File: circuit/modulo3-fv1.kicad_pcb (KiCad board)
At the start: 2 copper layers, 90 x 80 mm, 55 parts, among them J1 CONN_01X04, J2 CONN_01X10, J3 CONN_01X03, J4 HOLE, J5 HOLE, U1 OPA1642, U10 TLE2426, U2 PWR_CONN, U3 FV-1, U5 LM1117 3V3, U7 AD5142A, Y1 32768Hz

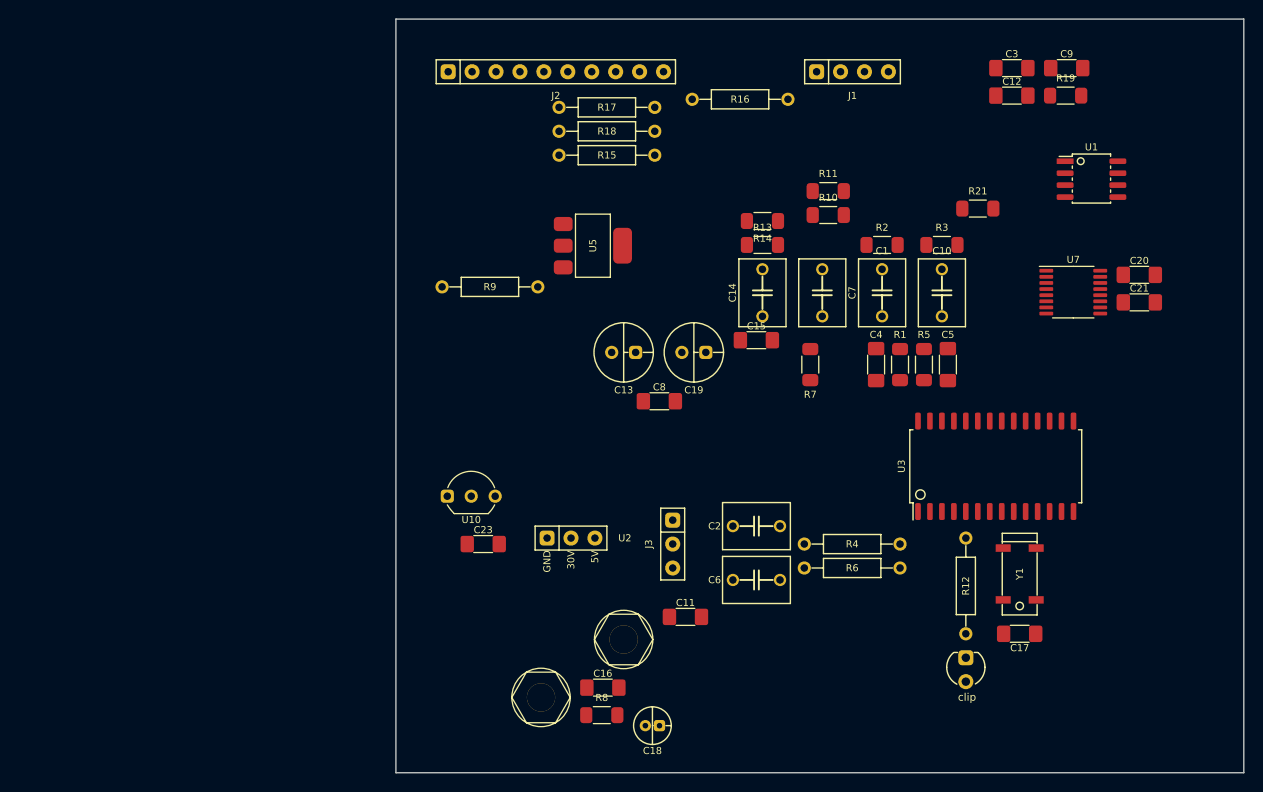
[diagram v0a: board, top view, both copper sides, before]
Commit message: mcu board; fv1 board tracing
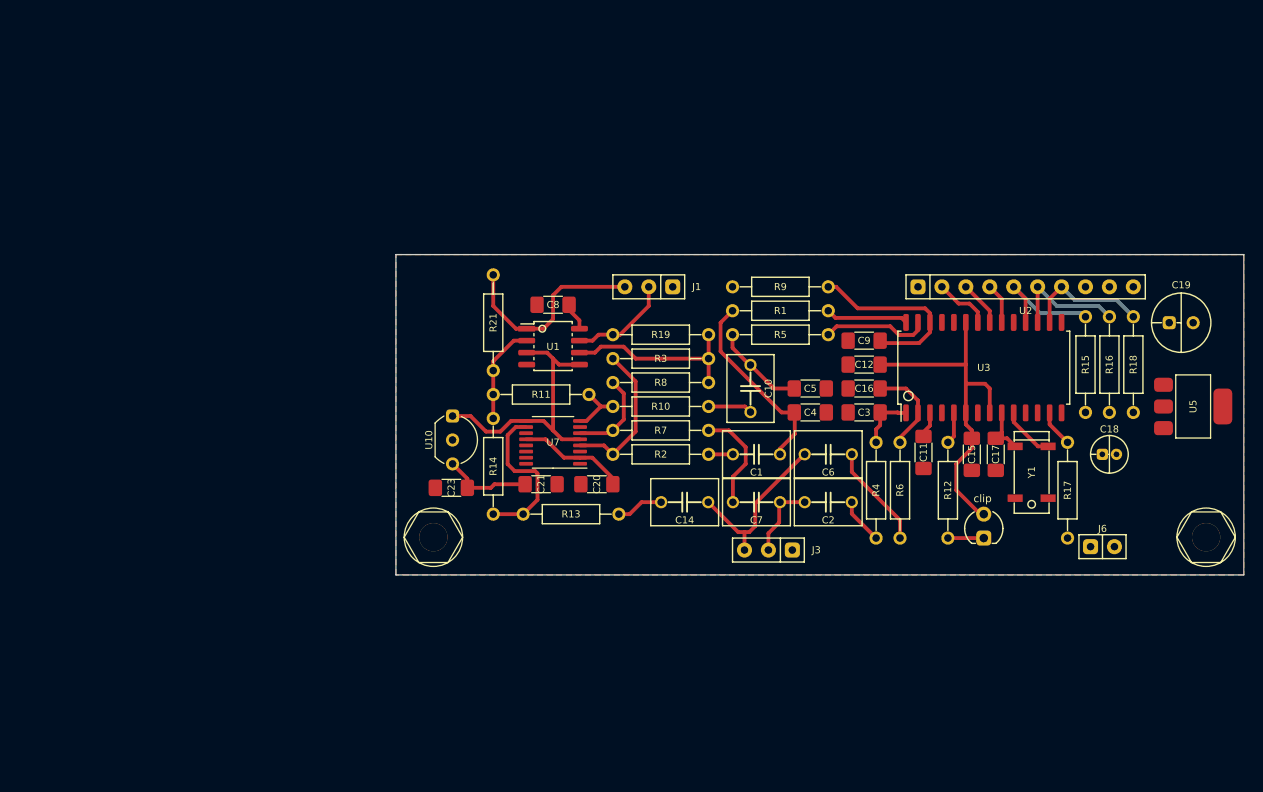
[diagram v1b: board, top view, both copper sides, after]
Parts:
- removed C13: 10µF, myAmp:CPOL_D6.3_P2.5
- removed J2: CONN_01X10, myAmp:PIN_1x10
- added J6: CONN_01X02, myAmp:PIN_1x02, F.Cu at (165.0, 86.0)
- J1: value CONN_01X04 -> CONN_01X03; footprint myAmp:PIN_1x04 -> myAmp:PIN_1x03
- R1, R10, R11, R13, R14, R19, R2, R21, R3, R5, R7, R8: footprint myAmp:R_1206 -> myAmp:R_10MM
- U2: value PWR_CONN -> FV1_CONN; footprint myAmp:PWR_CONN -> myAmp:PIN_1x10
- moved C21 66.4 mm to (105.4, 79.4), turned to 180 degrees
- moved U5 66.0 mm to (174.6, 71.1)
- moved R17 63.6 mm to (161.3, 80.0), turned to -90 degrees
- moved J4 62.8 mm to (176.0, 85.0)
- moved C20 61.7 mm to (111.3, 79.4)
- moved R18 61.1 mm to (168.3, 66.7), turned to -90 degrees
- moved U1 59.9 mm to (106.7, 64.8)
- moved U7 57.5 mm to (106.7, 74.9), turned to 180 degrees
- moved C18 56.4 mm to (165.7, 76.2), turned to 180 degrees
- moved R15 55.4 mm to (163.2, 66.7), turned to -90 degrees
- moved U2 55.1 mm to (156.8, 58.4)
- moved R21 52.8 mm to (100.3, 62.2), turned to 90 degrees
- moved C19 51.8 mm to (173.4, 62.2), turned to 180 degrees
- moved R19 49.9 mm to (118.1, 63.5), turned to 180 degrees
- moved R16 48.3 mm to (165.7, 66.7), turned to 90 degrees
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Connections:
- J1 pad 3: GND -> /OUTR
- U2 pad 2: +24V -> /POT2
- U2 pad 3: +5V -> /POT1
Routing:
- net +3V3: track 0.00 -> 48.7 mm
- net VGND: track 0.00 -> 29.2 mm
- net /OUTR: track 0.00 -> 21.6 mm
- net /FVL: track 0.00 -> 20.5 mm
- net /REFP: track 0.00 -> 19.8 mm
- net Net-(R19-Pad1): track 0.00 -> 19.6 mm
- net INR: track 0.00 -> 18.3 mm
- net /B2: track 0.00 -> 17.1 mm
- net /A1: track 0.00 -> 16.0 mm
- net /S2: track 0.00 -> 13.2 mm
- net /S0: track 0.00 -> 13.2 mm
- net /S1: track 0.00 -> 12.7 mm
- net +5V: track 0.00 -> 12.5 mm
- net Net-(R5-Pad2): track 0.00 -> 11.3 mm
- net Net-(C7-Pad2): track 0.00 -> 11.1 mm
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- added copper zone on F.Cu, net GND
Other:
- board size 90 x 80 mm -> 90 x 34 mm

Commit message: general layout and board sizes
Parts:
- U2: footprint myAmp:PIN_1x10 -> myAmp:FV1_CONN
- moved J5 26.0 mm to (94.0, 59.0)
- moved J4 26.0 mm to (176.0, 59.0)
- moved C19 8.89 mm to (173.4, 71.1)
- moved U5 7.85 mm to (172.7, 78.7)
- moved U2 5.85 mm to (151.1, 57.1), turned to -90 degrees
- moved R13 2.36 mm to (108.6, 84.9)
- moved R21 1.91 mm to (100.3, 64.1)
- moved C1 1.91 mm to (128.3, 78.1)
- moved C10 1.91 mm to (127.6, 71.1)
- moved C11 1.91 mm to (146.0, 77.9)
- moved C12 1.91 mm to (139.7, 68.6)
- moved C14 1.91 mm to (120.7, 83.2)
- moved C15 1.91 mm to (151.1, 78.1)
- moved C16 1.91 mm to (139.7, 71.1)
- moved C17 1.91 mm to (153.7, 78.1)
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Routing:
- net /T0: track 3.92 -> 34.2 mm
- net /SCL: track 0.00 -> 17.3 mm
- net /S2: track 13.2 -> 27.7 mm
- net /S1: track 12.7 -> 26.0 mm
- net /S0: track 13.2 -> 25.5 mm
- net /SDA: track 0.00 -> 7.50 mm
- net /POT1: track 4.83 -> 12.0 mm
- net /POT2: track 6.03 -> 12.9 mm
- net /POT0: track 4.31 -> 11.1 mm
- net /B2: track 17.1 -> 17.7 mm
- net GND: vias 0 -> 3
- added copper zone on B.Cu, net GND

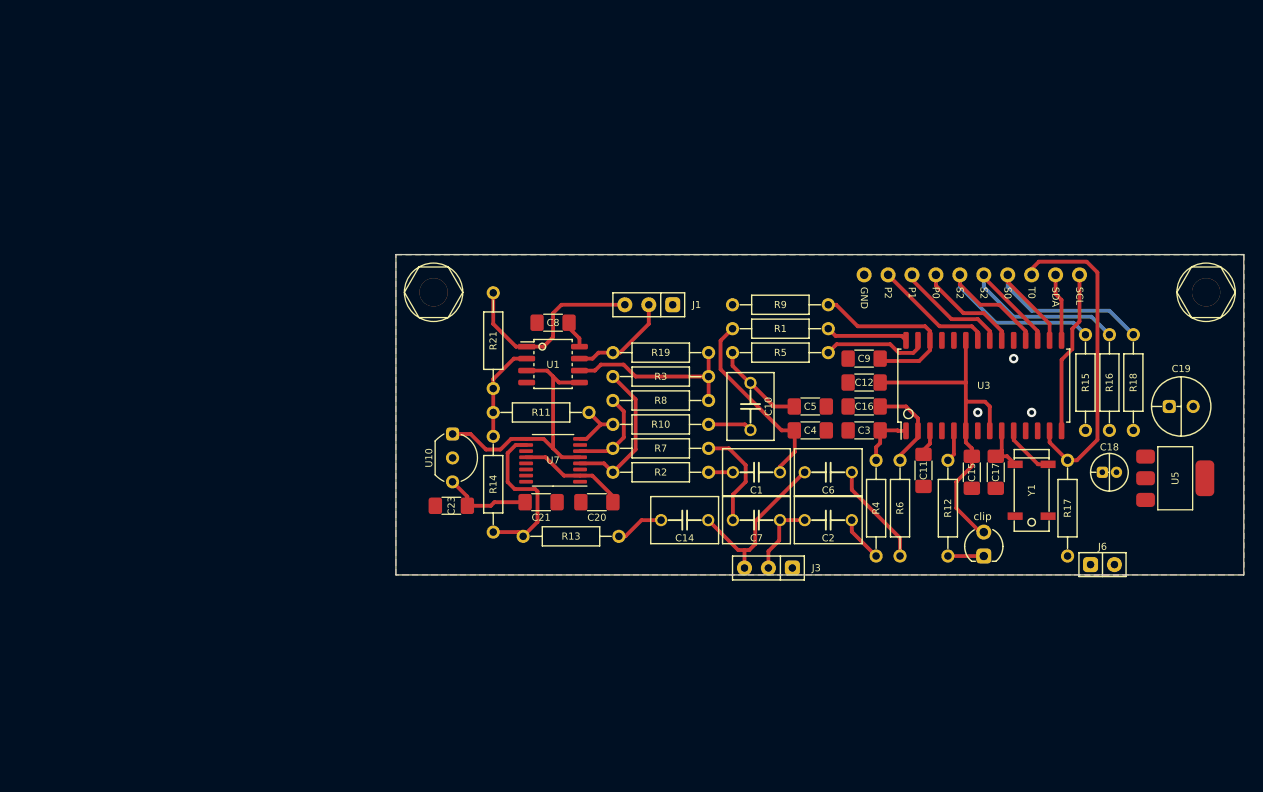
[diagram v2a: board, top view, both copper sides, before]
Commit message: got the pcs and holes sizes for mcu, poweamp and fv1
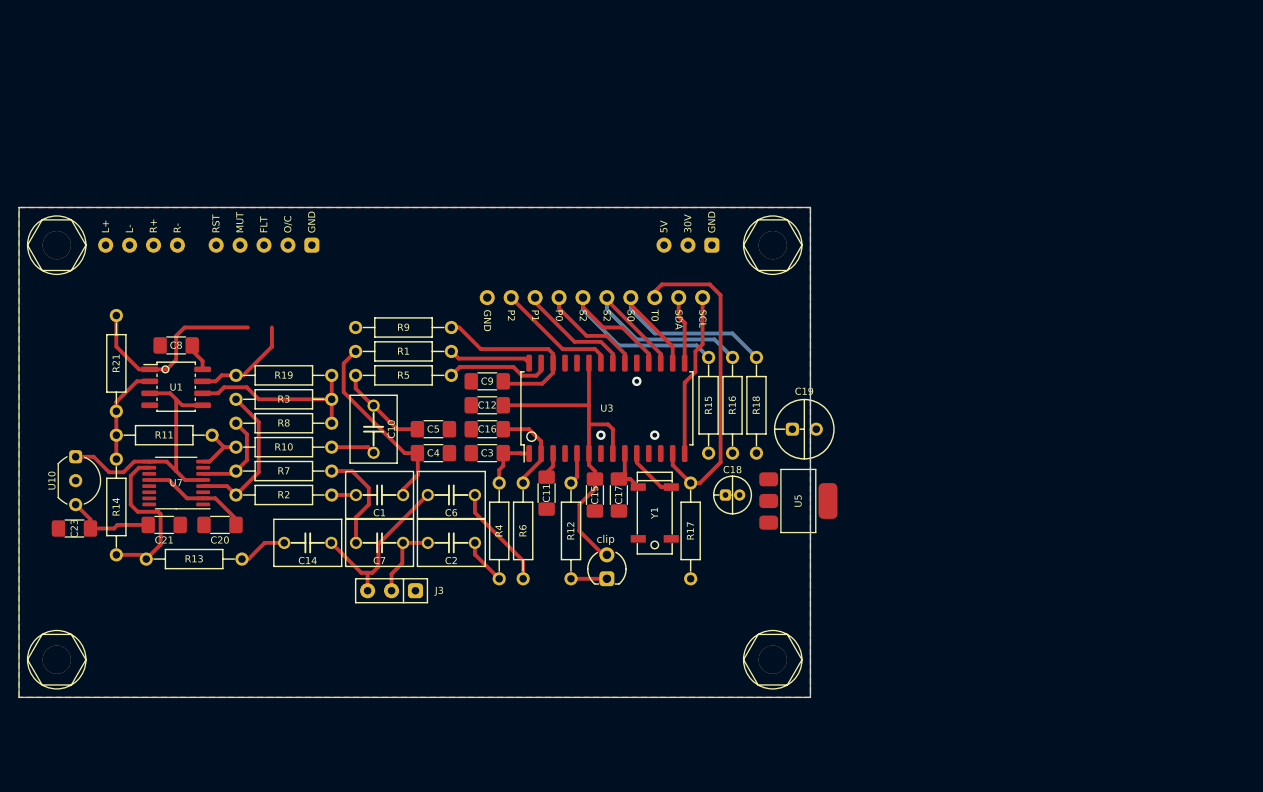
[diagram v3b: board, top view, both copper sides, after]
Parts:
- removed J1: CONN_01X03, myAmp:PIN_1x03
- removed J6: CONN_01X02, myAmp:PIN_1x02
- added J2: HOLE, myAmp:MountingHole, F.Cu at (54.0, 98.0)
- added J7: HOLE, myAmp:MountingHole, F.Cu at (130.0, 98.0)
- added U4: PWR_CONN, myAmp:PWR_CONN, F.Cu at (121.0, 54.0)
- added U6: DIFFAUDIO, myAmp:DIFFAUDIO, F.Cu at (63.0, 54.0)
- added U8: AMPCTRL, myAmp:AMPCTRL, F.Cu at (76.0, 54.0)
- moved J4 46.3 mm to (130.0, 54.0)
- moved J5 40.3 mm to (54.0, 54.0)
- moved C1 40.1 mm to (88.3, 80.5)
- moved C10 40.1 mm to (87.6, 73.5)
- moved C14 40.1 mm to (80.6, 85.6)
- moved C18 40.1 mm to (125.7, 80.5)
- moved C4 40.1 mm to (94.0, 76.1)
- moved C5 40.1 mm to (94.0, 73.5)
- moved C7 40.1 mm to (88.3, 85.6)
- moved C8 40.1 mm to (66.7, 64.6)
- moved D1 40.1 mm to (112.4, 88.1)
- moved R12 40.1 mm to (108.6, 84.3)
- moved R16 40.1 mm to (125.7, 71.0)
- moved U1 40.1 mm to (66.7, 69.1)
- moved U3 40.1 mm to (112.4, 71.3)
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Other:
- board size 90 x 34 mm -> 84 x 52 mm

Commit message: fv-1 mostly done; power progressed
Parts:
- removed J3: CONN_01X03, myAmp:PIN_1x03
- added U9: PREAMP, myAmp:PREAMP_CONN, F.Cu at (80.0, 98.0)
- moved R16 36.4 mm to (92.1, 57.1), turned to 0 degrees
- moved R15 33.1 mm to (92.1, 59.7), turned to 180 degrees
- moved R18 25.1 mm to (107.3, 57.1), turned to 0 degrees
- moved C18 22.2 mm to (120.2, 59.0), turned to 0 degrees
- moved U5 16.1 mm to (125.0, 67.0), turned to -90 degrees
- moved C14 15.7 mm to (66.6, 92.7)
- moved R13 13.3 mm to (55.2, 87.0), turned to 90 degrees
- moved U2 11.6 mm to (101.0, 54.0), turned to 0 degrees
- moved R14 9.05 mm to (55.2, 74.3)
- moved C19 8.63 mm to (125.0, 75.7), turned to -90 degrees
- moved U10 8.27 mm to (64.1, 77.5), turned to 180 degrees
- moved C23 7.90 mm to (59.1, 76.8), turned to 90 degrees
- moved C21 7.12 mm to (58.4, 85.1), turned to 90 degrees
- moved U7 5.23 mm to (64.1, 83.8)
- moved C7 4.58 mm to (85.1, 88.9)
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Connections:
- R12 pad 2: Net-(R12-Pad2) -> /CLIP
- U2 pad 1: GND -> /POT2
- U2 pad 10: /SCL -> /CLIP
- U2 pad 2: /POT2 -> /POT1
- U2 pad 3: /POT1 -> /POT0
- U2 pad 4: /POT0 -> /S2
- U2 pad 5: /S2 -> /S1
- U2 pad 6: /S1 -> /S0
- U2 pad 7: /S0 -> /FV_SDA
- U2 pad 8: /T0 -> /FV_SCL
- U2 pad 9: /SDA -> /T0
- U3 pad 14: /SCL -> /FV_SCL
- U3 pad 15: /SDA -> /FV_SDA
- U3 pad 5: Net-(R12-Pad2) -> /CLIP
- U4 pad 2: unconnected-(U4-Pad2) -> /30V
- U7 pad 13: /SCL -> SCL
- U7 pad 14: /SDA -> SDA
- U8 pad 1: unconnected-(U8-Pad1) -> GND
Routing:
- net /30V: track 0.00 -> 86.9 mm
- net +5V: track 12.5 -> 95.3 mm
- net +3V3: track 48.7 -> 116.8 mm
- net /CLIP: track 0.00 -> 60.4 mm
- net /FV_SCL: track 0.00 -> 28.4 mm
- net INR: track 18.3 -> 45.7 mm
- net SCL: track 0.00 -> 22.8 mm
- net SDA: track 0.00 -> 20.0 mm
- net /FV_SDA: track 0.00 -> 19.5 mm
- net /SCL: track 17.3 -> 0.00 mm
- net /POT0: track 11.1 -> 27.6 mm
- net /POT1: track 12.0 -> 28.0 mm
- net /POT2: track 12.9 -> 28.4 mm
- net /B2: track 17.7 -> 8.68 mm
- net /OUTL: track 10.9 -> 19.0 mm
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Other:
- outline, holes or cut-outs redrawn

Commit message: lotsa things :)
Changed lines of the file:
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@@
         (effects (font (size 0.75 0.75) (thickness 0.15)))
     )
-    (fp_text user "CLP" (at 11.43 -1.27 90 unlocked) (layer "F.SilkS")
+    (fp_text user "T0" (at 8.89 -1.27 90 unlocked) (layer "F.SilkS")
+        (effects (font (size 0.75 0.75) (thickness 0.15)) (justify left))
+    )
+    (fp_text user "SDA" (at 3.81 -1.27 90 unlocked) (layer "F.SilkS")
+        (effects (font (size 0.75 0.75) (thickness 0.15)) (justify left))
+    )
+    (fp_text user "P1" (at -8.89 -1.27 90 unlocked) (layer "F.SilkS")
         (effects (font (size 0.75 0.75) (thickness 0.15)) (justify left))
     )
     (fp_text user "S0" (at 1.27 -1.27 90 unlocked) (layer "F.SilkS")
-        (effects (font (size 0.75 0.75) (thickness 0.15)) (justify left))
-    )
-    (fp_text user "P0" (at -6.35 -1.27 90 unlocked) (layer "F.SilkS")
         (effects (font (size 0.75 0.75) (thickness 0.15)) (justify left))
     )
@@
         (effects (font (size 0.75 0.75) (thickness 0.15)) (justify left))
     )
-    (fp_text user "P1" (at -8.89 -1.27 90 unlocked) (layer "F.SilkS")
-        (effects (font (size 0.75 0.75) (thickness 0.15)) (justify left))
-    )
-    (fp_text user "T0" (at 8.89 -1.27 90 unlocked) (layer "F.SilkS")
-        (effects (font (size 0.75 0.75) (thickness 0.15)) (justify left))
-    )
-    (fp_text user "SDA" (at 3.81 -1.27 90 unlocked) (layer "F.SilkS")
-        (effects (font (size 0.75 0.75) (thickness 0.15)) (justify left))
-    )
     (fp_text user "S2" (at -3.81 -1.27 90 unlocked) (layer "F.SilkS")
         (effects (font (size 0.75 0.75) (thickness 0.15)) (justify left))
     )
-    (pad "1" thru_hole circle (at -11.43 0) (size 1.6 1.6) (drill 0.9) (layers "*.Cu" "*.Mask")
+    (fp_text user "CLP" (at 11.43 -1.27 90 unlocked) (layer "F.SilkS")
+        (effects (font (size 0.75 0.75) (thickness 0.15)) (justify left))
+    )
+    (fp_text user "P0" (at -6.35 -1.27 90 unlocked) (layer "F.SilkS")
+        (effects (font (size 0.75 0.75) (thickness 0.15)) (justify left))
+    )
+    (pad "1" thru_hole circle (at -11.43 0) (size 1.6 1.6) (drill 0.8) (layers "*.Cu" "*.Mask")
       (net 24 "/POT2") (pinfunction "POT2") (pintype "input"))
-    (pad "2" thru_hole circle (at -8.89 0) (size 1.6 1.6) (drill 0.9) (layers "*.Cu" "*.Mask")
+    (pad "2" thru_hole circle (at -8.89 0) (size 1.6 1.6) (drill 0.8) (layers "*.Cu" "*.Mask")
       (net 23 "/POT1") (pinfunction "POT1") (pintype "input"))
-    (pad "3" thru_hole circle (at -6.35 0) (size 1.6 1.6) (drill 0.9) (layers "*.Cu" "*.Mask")
+    (pad "3" thru_hole circle (at -6.35 0) (size 1.6 1.6) (drill 0.8) (layers "*.Cu" "*.Mask")
       (net 22 "/POT0") (pinfunction "POT0") (pintype "input"))
-    (pad "4" thru_hole circle (at -3.81 0) (size 1.6 1.6) (drill 0.9) (layers "*.Cu" "*.Mask")
+    (pad "4" thru_hole circle (at -3.81 0) (size 1.6 1.6) (drill 0.8) (layers "*.Cu" "*.Mask")
       (net 27 "/S2") (pinfunction "S2") (pintype "input"))
-    (pad "5" thru_hole circle (at -1.27 0) (size 1.6 1.6) (drill 0.9) (layers "*.Cu" "*.Mask")
+    (pad "5" thru_hole circle (at -1.27 0) (size 1.6 1.6) (drill 0.8) (layers "*.Cu" "*.Mask")
       (net 26 "/S1") (pinfunction "S1") (pintype "input"))
-    (pad "6" thru_hole circle (at 1.27 0) (size 1.6 1.6) (drill 0.9) (layers "*.Cu" "*.Mask")
+    (pad "6" thru_hole circle (at 1.27 0) (size 1.6 1.6) (drill 0.8) (layers "*.Cu" "*.Mask")
       (net 25 "/S0") (pinfunction "S0") (pintype "input"))
-    (pad "7" thru_hole circle (at 3.81 0) (size 1.6 1.6) (drill 0.9) (layers "*.Cu" "*.Mask")
+    (pad "7" thru_hole circle (at 3.81 0) (size 1.6 1.6) (drill 0.8) (layers "*.Cu" "*.Mask")
       (net 29 "/FV_SDA") (pinfunction "SDA") (pintype "input"))
-    (pad "8" thru_hole circle (at 6.35 0) (size 1.6 1.6) (drill 0.9) (layers "*.Cu" "*.Mask")
+    (pad "8" thru_hole circle (at 6.35 0) (size 1.6 1.6) (drill 0.8) (layers "*.Cu" "*.Mask")
       (net 30 "/FV_SCL") (pinfunction "SCL") (pintype "input"))
-    (pad "9" thru_hole circle (at 8.89 0) (size 1.6 1.6) (drill 0.9) (layers "*.Cu" "*.Mask")
+    (pad "9" thru_hole circle (at 8.89 0) (size 1.6 1.6) (drill 0.8) (layers "*.Cu" "*.Mask")
       (net 28 "/T0") (pinfunction "T0") (pintype "input"))
-    (pad "10" thru_hole circle (at 11.43 0) (size 1.6 1.6) (drill 0.9) (layers "*.Cu" "*.Mask")
+    (pad "10" thru_hole circle (at 11.43 0) (size 1.6 1.6) (drill 0.8) (layers "*.Cu" "*.Mask")
       (net 42 "/CLIP") (pinfunction "CLP") (pintype "input"))
     (model "${KIPRJMOD}/myAmp.pretty/models/PinHeader_1x10_P2.54mm_Vertical.step"
